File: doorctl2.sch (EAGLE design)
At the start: 48 parts, among them IC1 MEGA8-P, IC2 AT24CP, Q1 FDS5680, Q2 FDS5680, Q3 FDS5680, Q4 FDS5680, SW1 L202011MS02Q, SW2 L202011MS02Q

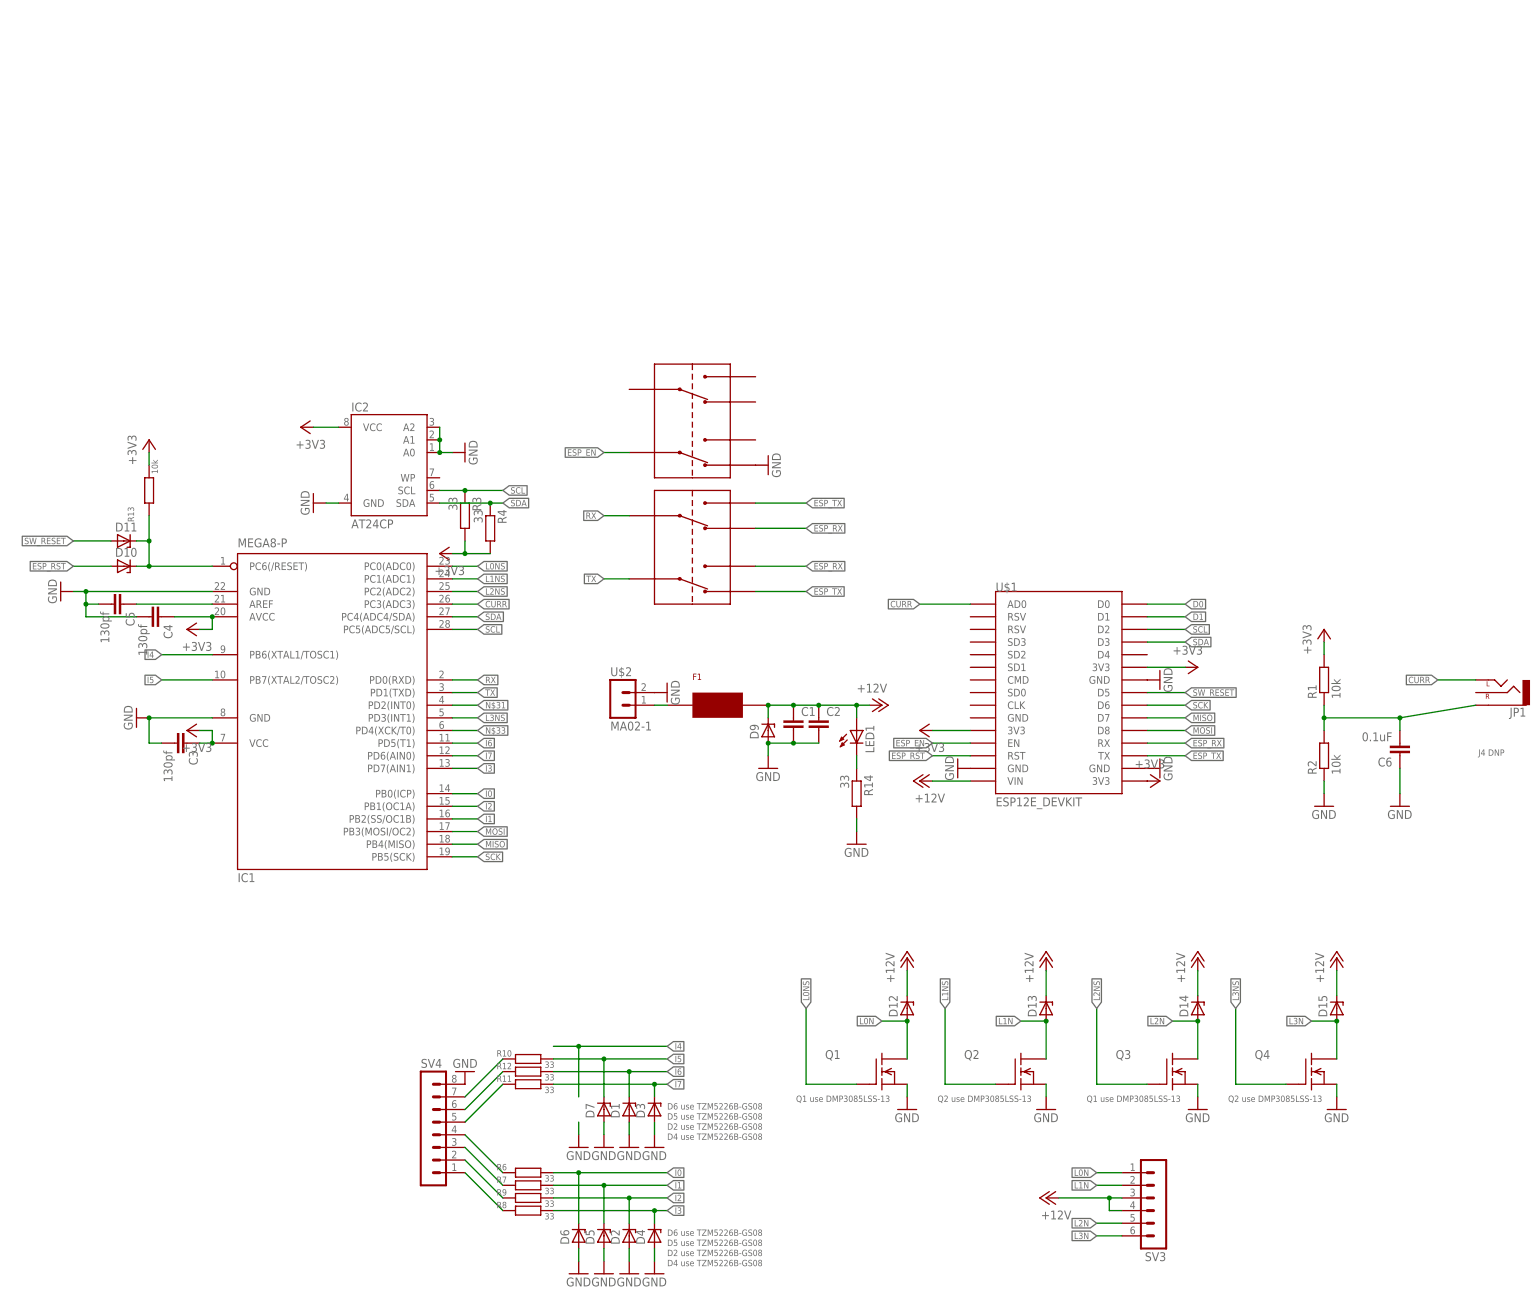
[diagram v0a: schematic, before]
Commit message: cleaned iup schem, added zener
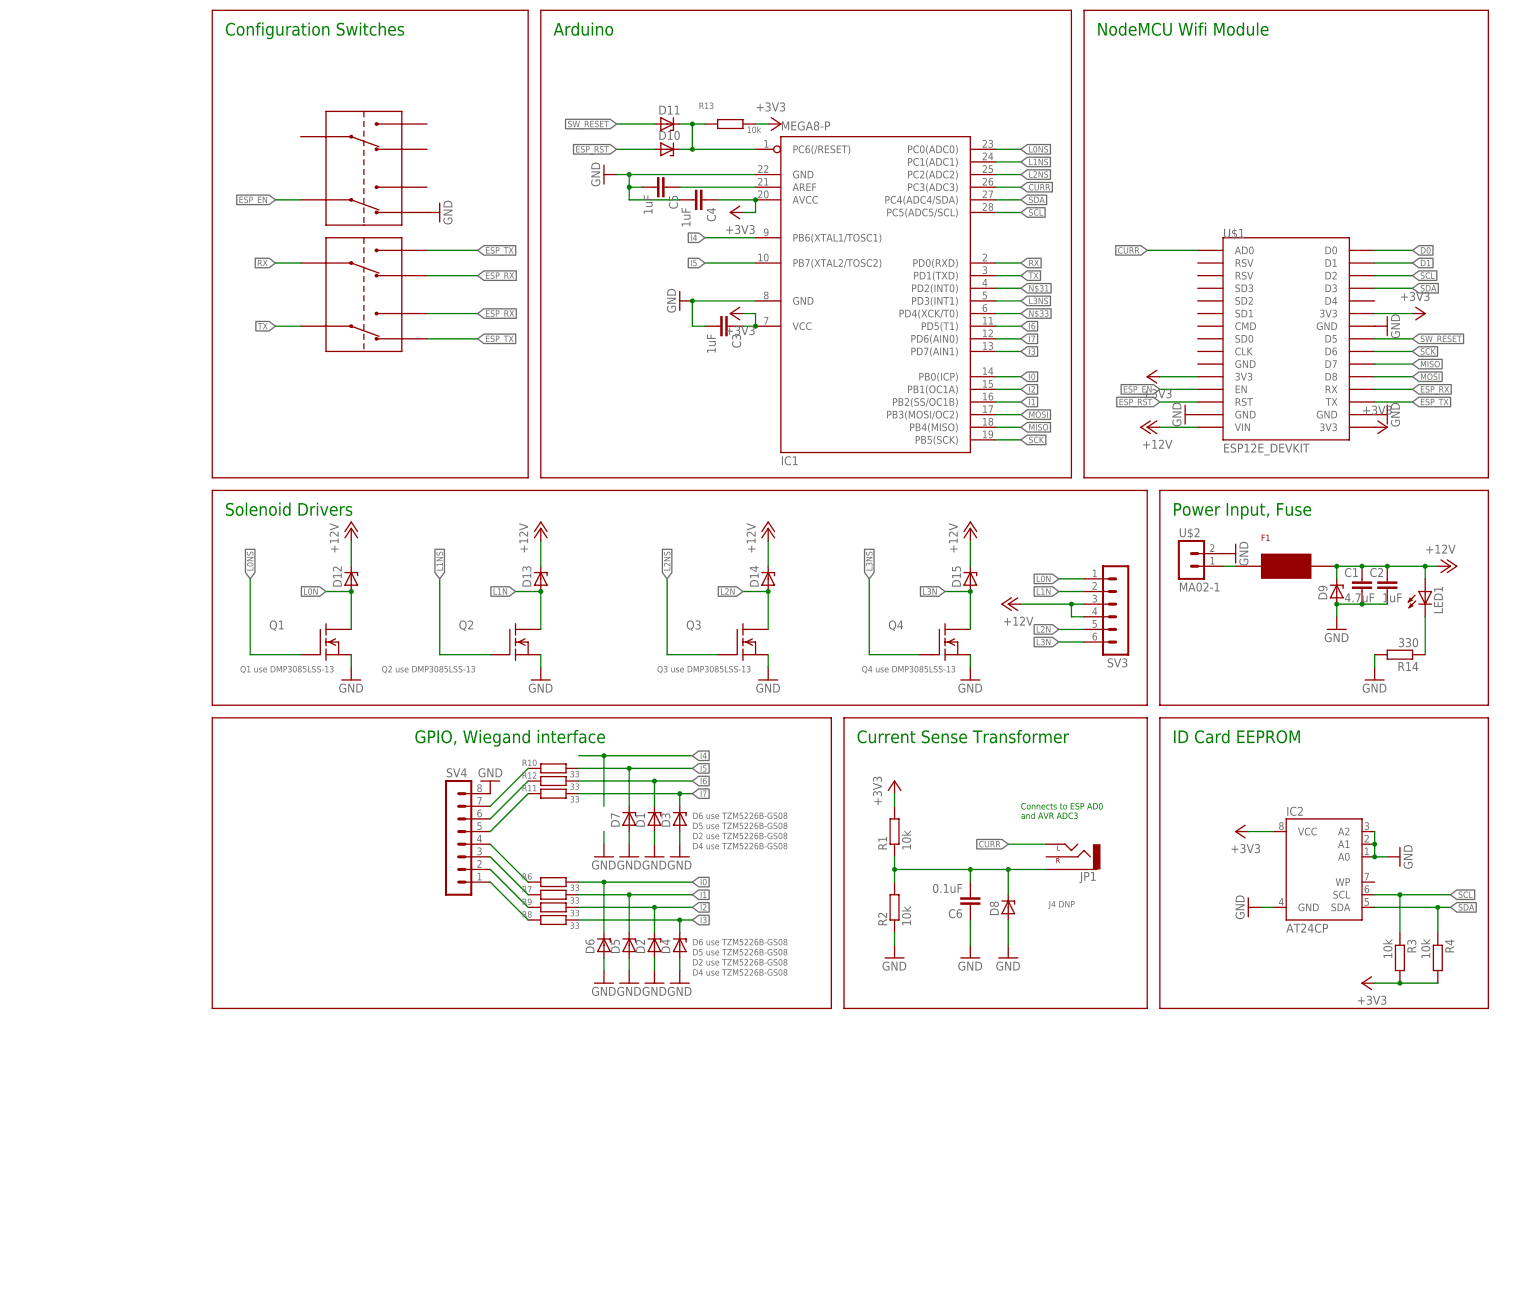
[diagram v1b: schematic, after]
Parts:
- added D8: (no value), diode:ZENER-DIODESOD80C
- C1: value (none) -> 4.7uF
- C2: value (none) -> 1uF
- C3, C4, C5: value 130pf -> 1uF
- R14: value 33 -> 330
- R3, R4: value 33 -> 10k
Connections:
- net GND: now also D8.A
- net N$12: now also D8.C
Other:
- note added: "Arduino"
- note added: "Configuration Switches"
- note added: "Connects to ESP AD0 and AVR ADC3"
- note added: "Current Sense Transformer"
- note added: "GPIO, Wiegand interface"
- note added: "ID Card EEPROM"
- note added: "NodeMCU Wifi Module"
- note added: "Power Input, Fuse"
- note added: "Q3 use DMP3085LSS-13"
- note added: "Q4 use DMP3085LSS-13"
- note added: "Solenoid Drivers"
- moved on the sheet: C1, C2, C3, C4, C5, C6, D1, D10, D11, D12, D13, D14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
